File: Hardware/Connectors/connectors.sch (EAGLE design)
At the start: 14 parts, among them X1 KUSBVX, X2 KUSBVX, X3 5566-2

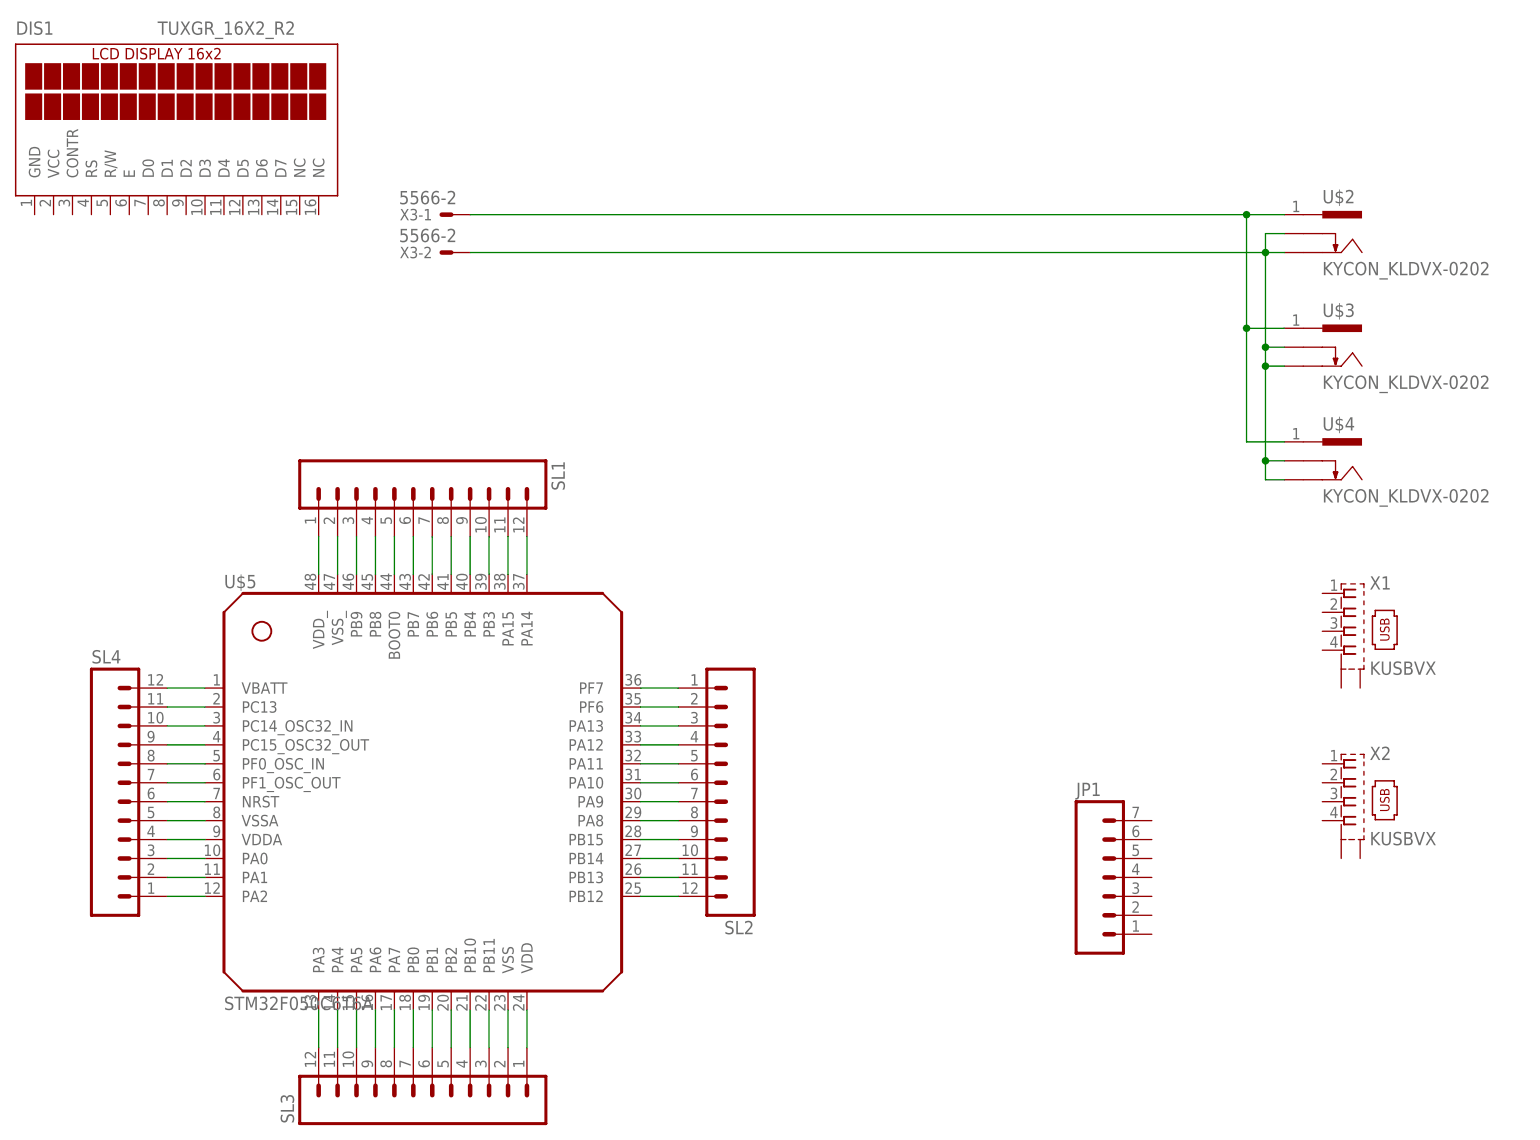
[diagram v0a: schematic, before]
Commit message: First Version of Standalone Connectors Layout
Prototype Faceplate is being designed based on this layout.
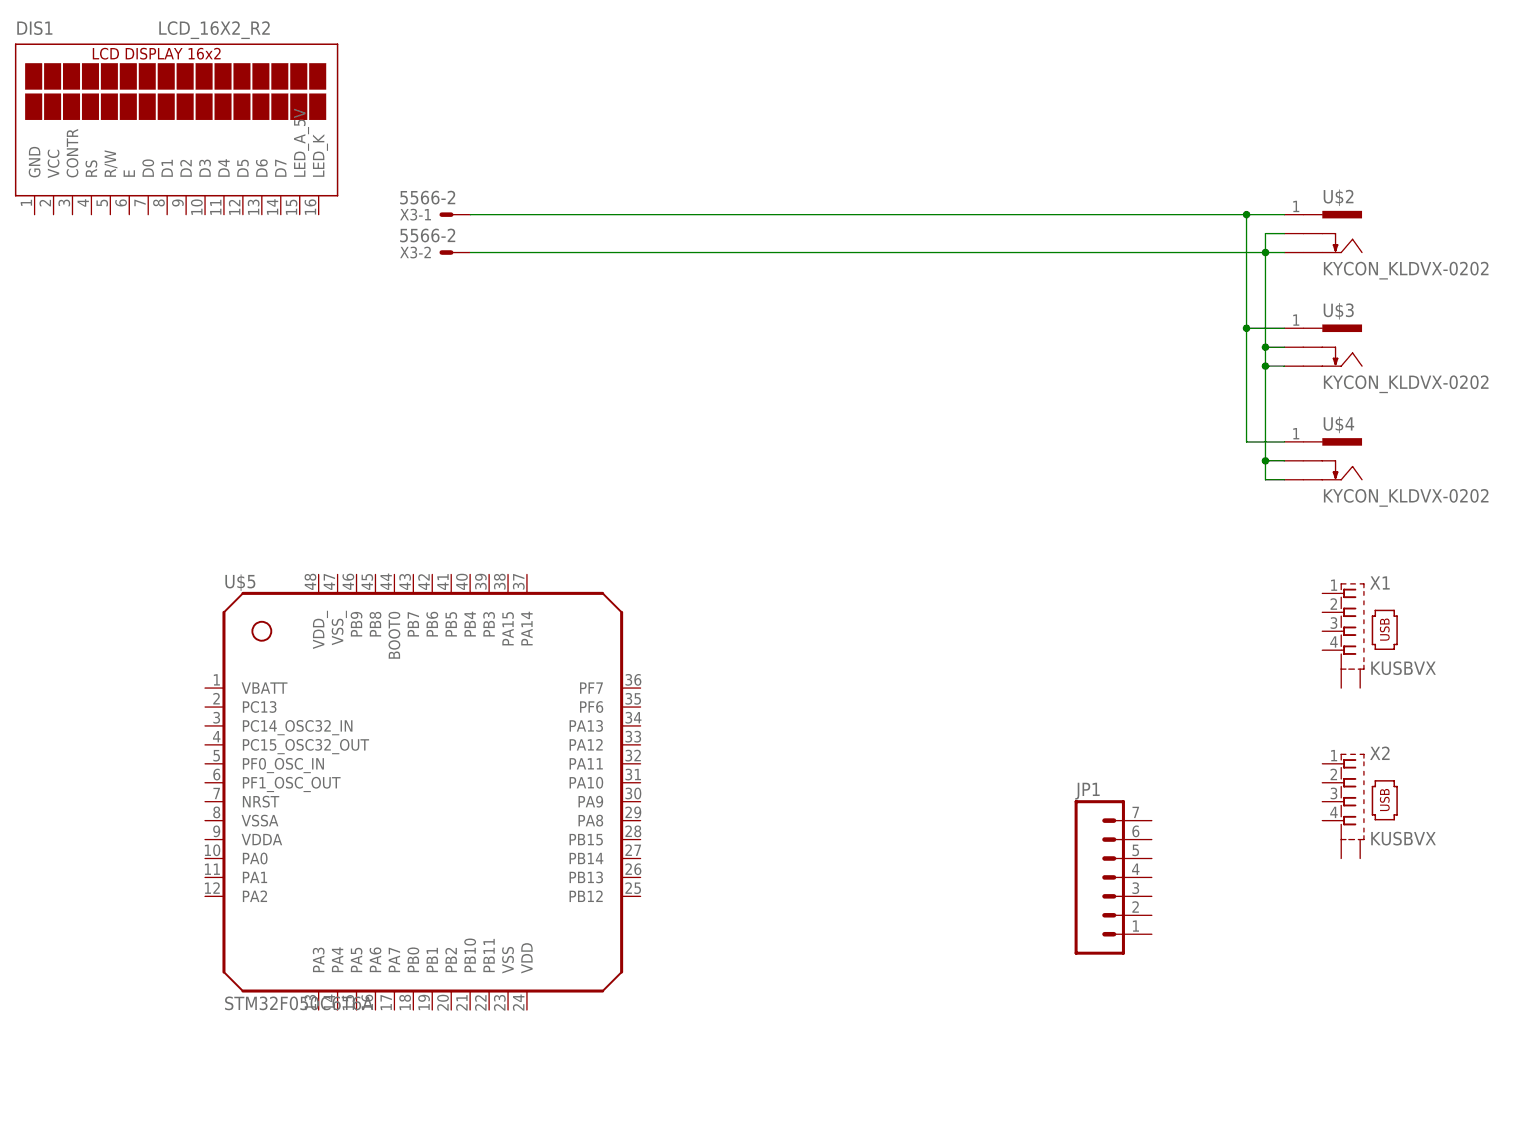
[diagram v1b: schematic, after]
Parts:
- removed SL1, SL2, SL3, SL4: (no value), con-amp-quick:M12
- DIS1: value TUXGR_16X2_R2 -> LCD_16X2_R2; device display-lcd:TUXGR_16X2_R2 -> equinox:LCD_16X2_R2
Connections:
- removed net N$10: SL1.8, U$5.PB5
- removed net N$11: SL1.9, U$5.PB4
- removed net N$12: SL1.10, U$5.PB3
- removed net N$13: SL1.11, U$5.PA15
- removed net N$14: SL1.12, U$5.PA14
- removed net N$15: SL4.12, U$5.VBATT
- removed net N$16: SL4.11, U$5.PC13
- removed net N$17: SL4.9, U$5.PC15_OSC32_OUT
- removed net N$18: SL4.10, U$5.PC14_OSC32_IN
- removed net N$19: SL4.8, U$5.PF0_OSC_IN
- removed net N$20: SL4.7, U$5.PF1_OSC_OUT
- removed net N$21: SL4.6, U$5.NRST
- removed net N$22: SL4.4, U$5.VDDA
- removed net N$23: SL4.5, U$5.VSSA
- removed net N$24: SL4.3, U$5.PA0
- removed net N$25: SL4.2, U$5.PA1
- removed net N$26: SL4.1, U$5.PA2
- removed net N$27: SL3.12, U$5.PA3
- removed net N$28: SL3.11, U$5.PA4
- removed net N$29: SL3.10, U$5.PA5
- removed net N$3: SL1.1, U$5.VDD_
- removed net N$30: SL3.9, U$5.PA6
- removed net N$31: SL3.8, U$5.PA7
- removed net N$32: SL3.7, U$5.PB0
- removed net N$33: SL3.6, U$5.PB1
- removed net N$34: SL3.5, U$5.PB2
- removed net N$35: SL3.4, U$5.PB10
- removed net N$36: SL3.3, U$5.PB11
- removed net N$37: SL3.2, U$5.VSS
- removed net N$38: SL3.1, U$5.VDD
- removed net N$39: SL2.1, U$5.PF7
- removed net N$4: SL1.2, U$5.VSS_
- removed net N$40: SL2.2, U$5.PF6
- removed net N$41: SL2.3, U$5.PA13
- removed net N$42: SL2.4, U$5.PA12
- removed net N$43: SL2.5, U$5.PA11
- removed net N$44: SL2.6, U$5.PA10
- removed net N$45: SL2.7, U$5.PA9
- removed net N$46: SL2.8, U$5.PA8
- removed net N$47: SL2.9, U$5.PB15
- removed net N$48: SL2.10, U$5.PB14
- removed net N$49: SL2.11, U$5.PB13
- removed net N$5: SL1.3, U$5.PB9
- removed net N$50: SL2.12, U$5.PB12
- removed net N$6: SL1.4, U$5.PB8
- removed net N$7: SL1.5, U$5.BOOT0
- removed net N$8: SL1.6, U$5.PB7
- removed net N$9: SL1.7, U$5.PB6
